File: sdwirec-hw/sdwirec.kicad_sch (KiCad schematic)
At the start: 60 parts, among them IC1 USB2640-HZH-02, IC2 MC74HC1G04DTT1G, J1 USB_C_Receptacle_USB2.0, J2 usd_plug, J3 Micro_SD_Card, Q1 SMMBT4403L, Q2 SMMBT4403L, U1 M24C02-RDW, U2 SPX3819M5-L-3-3, U3 TS3A27518EPW, U4 FT200XD, Y1 24Mhz

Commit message: Rev 1.2
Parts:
- added C26, C27: 4.7uF, Capacitor_SMD:C_0603_1608Metric, symbol Device:C_Small
- added C28, C29: 100nF, Capacitor_SMD:C_0402_1005Metric, symbol Device:C_Small
- added R18: 1M, Resistor_SMD:R_0402_1005Metric, symbol Device:R_Small
- added R19: 0R, Resistor_SMD:R_0402_1005Metric, symbol Device:R_Small
- C1, C14, C15, C20, C4: JLC (none) -> 0603
- C10, C11, C12, C13, C16, C17, C18, C19, C2, C21, C22, C23, C25, C3, C5, C6, C7, C9, D2, D4, R1, R10, R11, R12, R13, R14, R15, R16, R17, R2, R3, R4, R5, R6, R7, R8, R9: JLC (none) -> 0402
- C24, C8: JLC (none) -> CASE-A-3216
- D1: value LED_Small -> Red; JLC (none) -> 0402
- D3: value Green -> Blue; JLC (none) -> 0402
- FB1, FB2: value 180R -> 150R; footprint LED_SMD:LED_0603_1608Metric -> Diode_SMD:D_0603_1608Metric; JLC (none) -> 0603
- IC1: JLC (none) -> QFN-48-EP(7x7)
- IC2: JLC (none) -> SOT-23-5; LCSC Part (none) -> C154774
- J1: JLC (none) -> SMD; LCSC Part (none) -> C668624
- J3: LCSC Part (none) -> C587953
- Q1, Q2: JLC (none) -> SOT-23-3; LCSC Part (none) -> C231272
- U1: JLC (none) -> TSSOP-8-3.0mm; LCSC Part (none) -> C152731
- U2: JLC (none) -> SOT-23-5; LCSC Part (none) -> C9055
- U3: JLC (none) -> TSSOP-24; LCSC Part (none) -> C443721
- U4: JLC (none) -> DFN-10-EP(3x3); LCSC Part (none) -> C145361
- Y1: JLC (none) -> SMD3225-4P
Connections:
- net +3V3: now also C26.1, C27.1, C28.1
- net GND: now also C26.2, C27.2, C28.2, C29.2, R19.1
- net XTAL1: now also R18.2
- net XTAL2: now also R18.1
- net at J1.S1 (SHIELD), R9.1: now also C29.1
- net at IC1.13 (XD_D4_/_GPIO6_/_SD_WP_/_MS_SCLK): now also R19.2
- no-connect marks 24 -> 23
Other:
- moved on the sheet: C10, C14

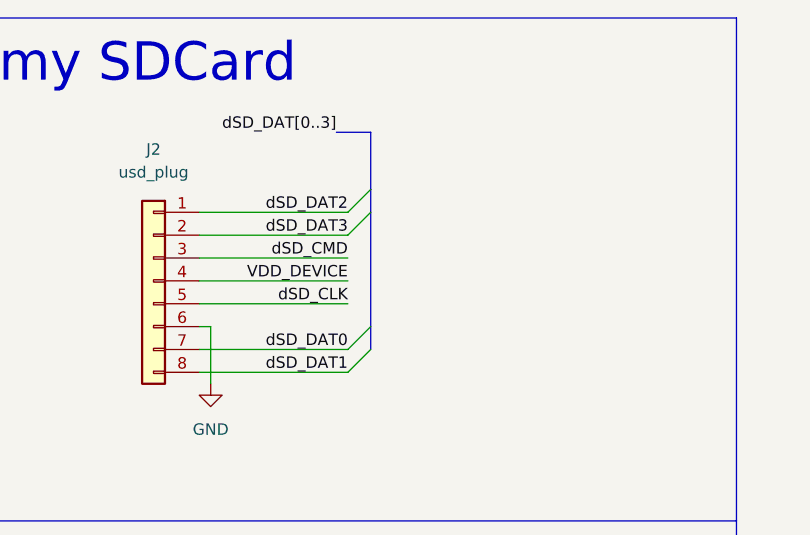
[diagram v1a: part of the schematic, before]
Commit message: add schottky diode on vdd_device line
Signed-off-by: Talha Can Havadar <havadartalha@gmail.com>
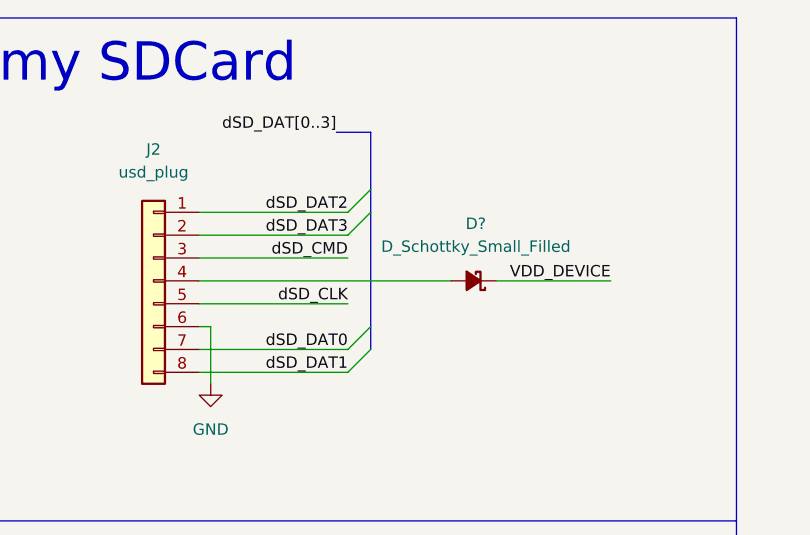
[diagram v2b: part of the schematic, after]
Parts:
- added D?: D_Schottky_Small_Filled, symbol Device:D_Schottky_Small_Filled
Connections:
- net VDD_DEVICE: now also D?.1 (K); no longer J2.4 (Pin_4)
- new net: D?.2 (A), J2.4 (Pin_4)
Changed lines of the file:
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@@
+    (stroke (width 0) (type default) (color 0 0 0 0))
+  )
+  (wire (pts (xy 284.48 41.91) (xy 297.18 41.91))
     (stroke (width 0) (type default) (color 0 0 0 0))
   )
@@
     (stroke (width 0) (type default) (color 0 0 0 0))
   )
-  (wire (pts (xy 251.46 41.91) (xy 267.97 41.91))
-    (stroke (width 0) (type default) (color 0 0 0 0))
-  )
   (wire (pts (xy 351.155 55.88) (xy 356.87 55.88))
     (stroke (width 0) (type default) (color 0 0 0 0))
@@
   )
   (wire (pts (xy 40.64 227.33) (xy 48.26 227.33))
+    (stroke (width 0) (type default) (color 0 0 0 0))
+  )
+  (wire (pts (xy 251.46 41.91) (xy 279.4 41.91))
     (stroke (width 0) (type default) (color 0 0 0 0))
   )
@@
     (effects (font (size 1.27 1.27)) (justify right bottom))
   )
-  (label "VDD_DEVICE" (at 267.97 41.91 180)
+  (label "VDD_DEVICE" (at 297.18 41.91 180)
     (effects (font (size 1.27 1.27)) (justify right bottom))
   )
@@
     (pin "1")
   )
+  (symbol (lib_id "Device:D_Schottky_Small_Filled") (at 281.94 41.91 180) (unit 1)
+    (in_bom yes) (on_board yes) (fields_autoplaced)
+    (property "Reference" "D?" (id 0) (at 282.194 35.56 0))
+    (property "Value" "D_Schottky_Small_Filled" (id 1) (at 282.194 38.1 0))
+    (property "Footprint" "" (id 2) (at 281.94 41.91 90)
+      (effects (font (size 1.27 1.27)) hide)
+    )
+    (property "Datasheet" "~" (id 3) (at 281.94 41.91 90)
+      (effects (font (size 1.27 1.27)) hide)
+    )
+    (pin "1")
+    (pin "2")
+  )
   (symbol (lib_id "Device:C_Small") (at 257.175 179.705 0) (unit 1)
     (in_bom yes) (on_board yes) (fields_autoplaced)
@@
       (reference "D4") (unit 1) (value "Yellow") (footprint "LED_SMD:LED_0402_1005Metric")
     )
+    (path "/edb7c392-6167-4d1e-afda-3629607e52a5"
+      (reference "D?") (unit 1) (value "D_Schottky_Small_Filled") (footprint "")
+    )
     (path "/f27184be-59d2-4453-986f-21a7476ed0b7"

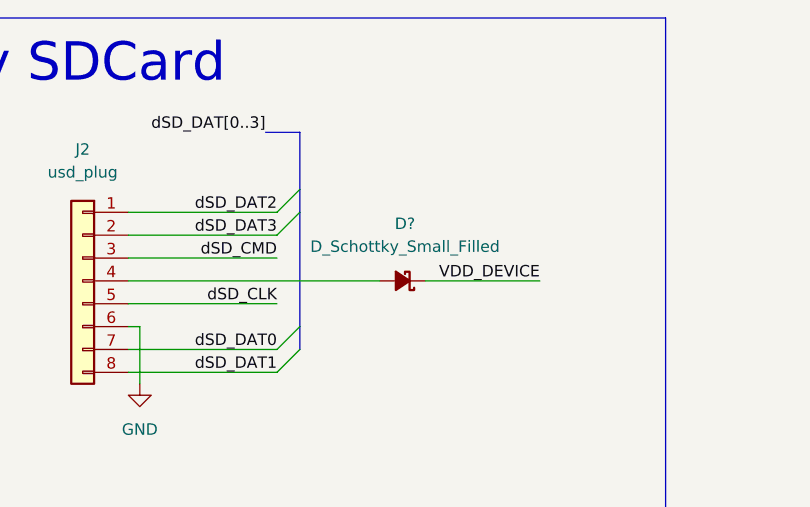
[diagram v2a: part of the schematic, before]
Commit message: squash! add schottky diode on vdd_device line
Signed-off-by: Talha Can Havadar <havadartalha@gmail.com>
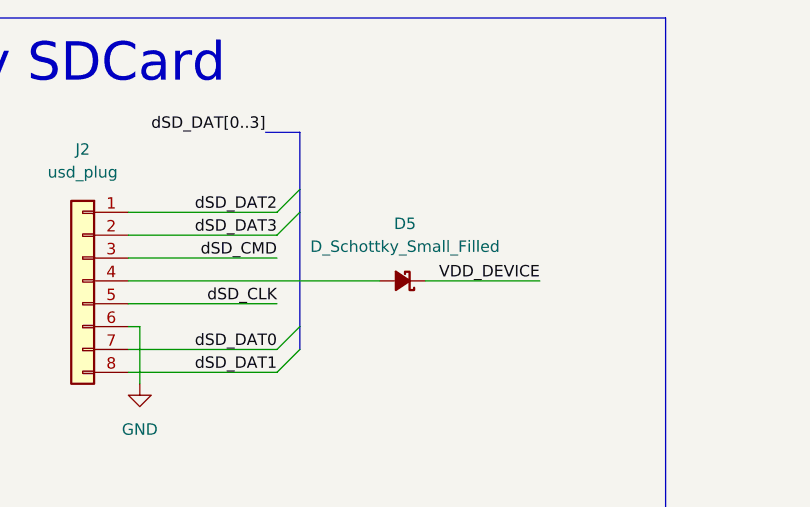
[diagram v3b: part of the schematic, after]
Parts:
- D5: renamed from D?; footprint (none) -> Diode_SMD:D_0402_1005Metric; LCSC Part (none) -> C2837790
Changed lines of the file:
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@@
   (symbol (lib_id "Device:D_Schottky_Small_Filled") (at 281.94 41.91 180) (unit 1)
     (in_bom yes) (on_board yes) (fields_autoplaced)
-    (property "Reference" "D?" (id 0) (at 282.194 35.56 0))
+    (property "Reference" "D5" (id 0) (at 282.194 35.56 0))
     (property "Value" "D_Schottky_Small_Filled" (id 1) (at 282.194 38.1 0))
-    (property "Footprint" "" (id 2) (at 281.94 41.91 90)
+    (property "Footprint" "Diode_SMD:D_0402_1005Metric" (id 2) (at 281.94 41.91 90)
       (effects (font (size 1.27 1.27)) hide)
     )
     (property "Datasheet" "~" (id 3) (at 281.94 41.91 90)
+      (effects (font (size 1.27 1.27)) hide)
+    )
+    (property "LCSC Part" "C2837790" (id 4) (at 281.94 41.91 0)
       (effects (font (size 1.27 1.27)) hide)
     )
@@
     )
     (path "/edb7c392-6167-4d1e-afda-3629607e52a5"
-      (reference "D?") (unit 1) (value "D_Schottky_Small_Filled") (footprint "")
+      (reference "D5") (unit 1) (value "D_Schottky_Small_Filled") (footprint "Diode_SMD:D_0402_1005Metric")
     )
     (path "/f27184be-59d2-4453-986f-21a7476ed0b7"
